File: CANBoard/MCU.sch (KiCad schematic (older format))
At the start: 23 parts, among them J5 SWD_10, U1 MCP2551, U2 STM32F303K8Tx, U3 MB85RC256V, Y1 8mHz

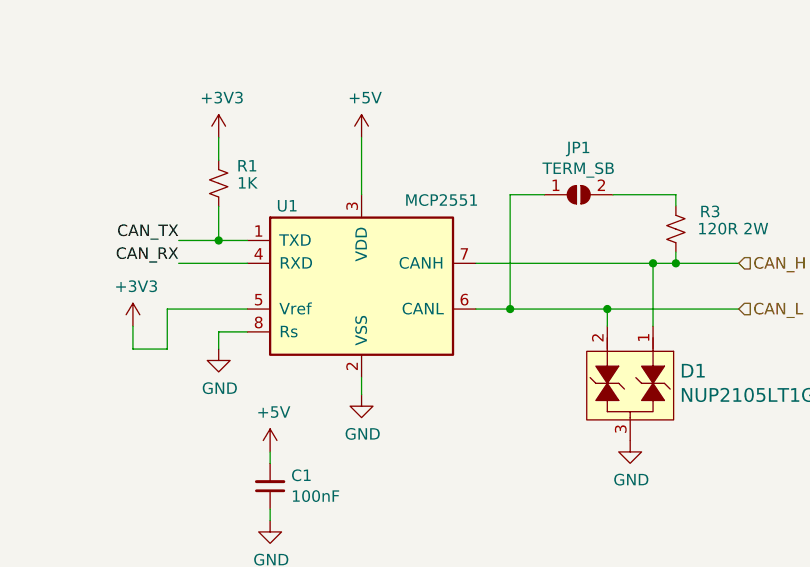
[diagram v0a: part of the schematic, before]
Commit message: Swapped MCP2551 to MCP2562
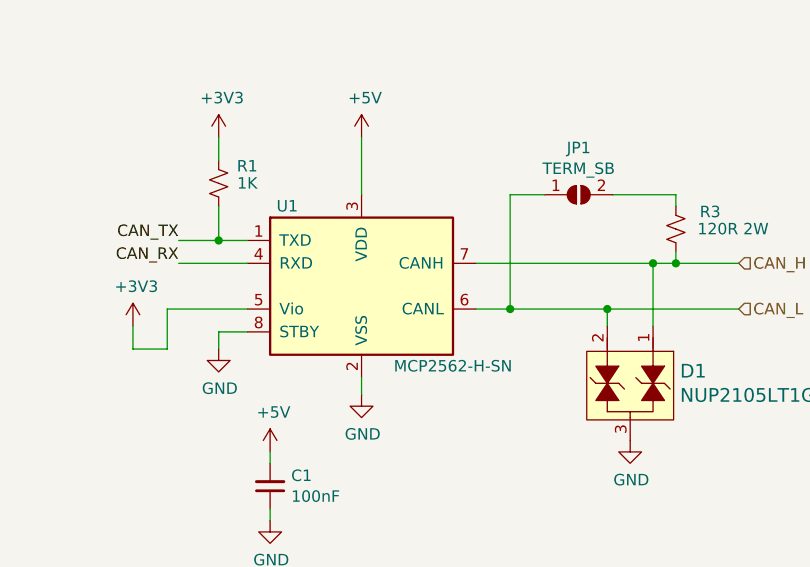
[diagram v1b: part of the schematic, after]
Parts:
- removed U1: MCP2551, Package_SO:SOIC-8_3.9x4.9mm_P1.27mm, symbol Interface_CAN_LIN:MCP2551-I-SN
- added U1: MCP2562-H-SN, Package_SO:SOIC-8_3.9x4.9mm_P1.27mm, symbol Interface_CAN_LIN:MCP2562-H-SN
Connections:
- net +3V3: now also U1.5 (Vio)
- net +5V: now also U1.3 (VDD)
- net CAN_H: now also U1.7 (CANH)
- net CAN_L: now also U1.6 (CANL)
- net CAN_RX: now also U1.4 (RXD)
- net CAN_TX: now also U1.1 (TXD)
- net GND: now also U1.2 (VSS), U1.8 (STBY)
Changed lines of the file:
@@
 Wire Wire Line
 	1350 6150 1350 6225
-$Comp
-L Interface_CAN_LIN:MCP2551-I-SN U1
-U 1 1 5FCD7BF5
-P 4300 6500
-F 0 "U1" H 3975 6850 50  0000 C CNN
-F 1 "MCP2551" H 4650 6875 50  0000 C CNN
-F 2 "Package_SO:SOIC-8_3.9x4.9mm_P1.27mm" H 4300 6000 50  0001 C CIN
-F 3 "http://ww1.microchip.com/downloads/en/devicedoc/21667d.pdf" H 4300 6500 50  0001 C CNN
-F 4 "MCP2551T-I/SNCT-ND" H 4300 6500 50  0001 C CNN "Digi-Key_PN"
-	1    4300 6500
-	1    0    0    -1
-$EndComp
 Text Label 6600 3225 0    50   ~ 0
 CAN_RX
@@
 Wire Wire Line
 	5225 3625 5275 3625
+$Comp
+L Interface_CAN_LIN:MCP2562-H-SN U1
+U 1 1 60AA37A8
+P 4300 6500
+F 0 "U1" H 3975 6850 50  0000 C CNN
+F 1 "MCP2562-H-SN" H 4700 6150 50  0000 C CNN
+F 2 "Package_SO:SOIC-8_3.9x4.9mm_P1.27mm" H 4300 6000 50  0001 C CIN
+F 3 "http://ww1.microchip.com/downloads/en/DeviceDoc/25167A.pdf" H 4300 6500 50  0001 C CNN
+	1    4300 6500
+	1    0    0    -1
+$EndComp
 $EndSCHEMATC
